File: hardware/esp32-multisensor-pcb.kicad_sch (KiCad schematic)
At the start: 19 parts, among them J1 SS-52400-002, J2 B2B-PH-SM4-TB, U2 MCP73871

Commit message: feat: add LDO voltage regulator and battery connector
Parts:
- added C3, C5: 0.1uF, symbol Device:C_Small
- added C4, C6: 10uF, symbol Device:C_Polarized_Small_US
- J2: value B2B-PH-SM4-TB -> LiPo
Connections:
- net +5V: now also VR1.3 (VIN), C3.1, C4.1
- net GND: now also J2.2, VR1.1 (GND), C3.2, C4.2, C5.2, C6.2
- net VBATT: now reaches U2.14 (V_{BAT}), U2.15 (V_{BAT}), U2.16 (V_{BAT_SENSE})
- net VBATT: now also J2.1
- net +3.3V: now reaches VR1.2 (VOUT_2)
- net +3.3V: now also VR1.4 (VOUT_4), C5.1, C6.1
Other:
- note added: "LiPo battery charger"
- note added: "Low Dropout(LDO)voltage regulator"
- note added: "USB connector"
- note removed: "LiPo Battery Charger"
- note removed: "USB Connector"
- moved on the sheet: D1, D2, D3, J2, R7, R8, R9

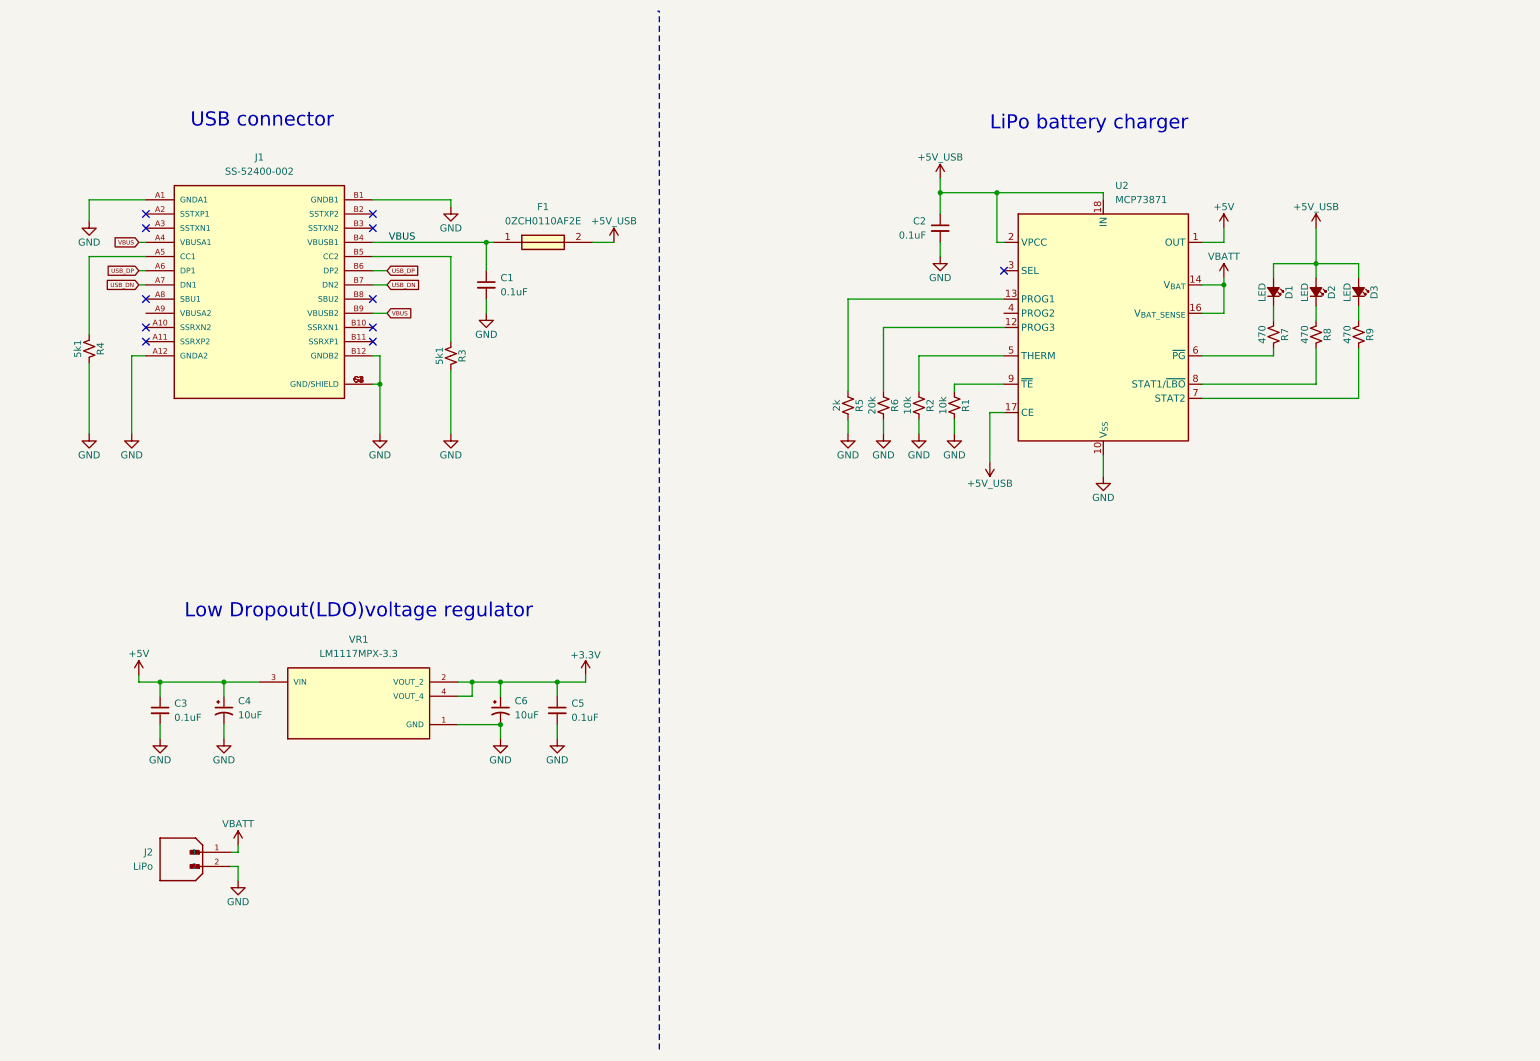
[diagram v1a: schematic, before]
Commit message: feat: add power LED indicator 3v3
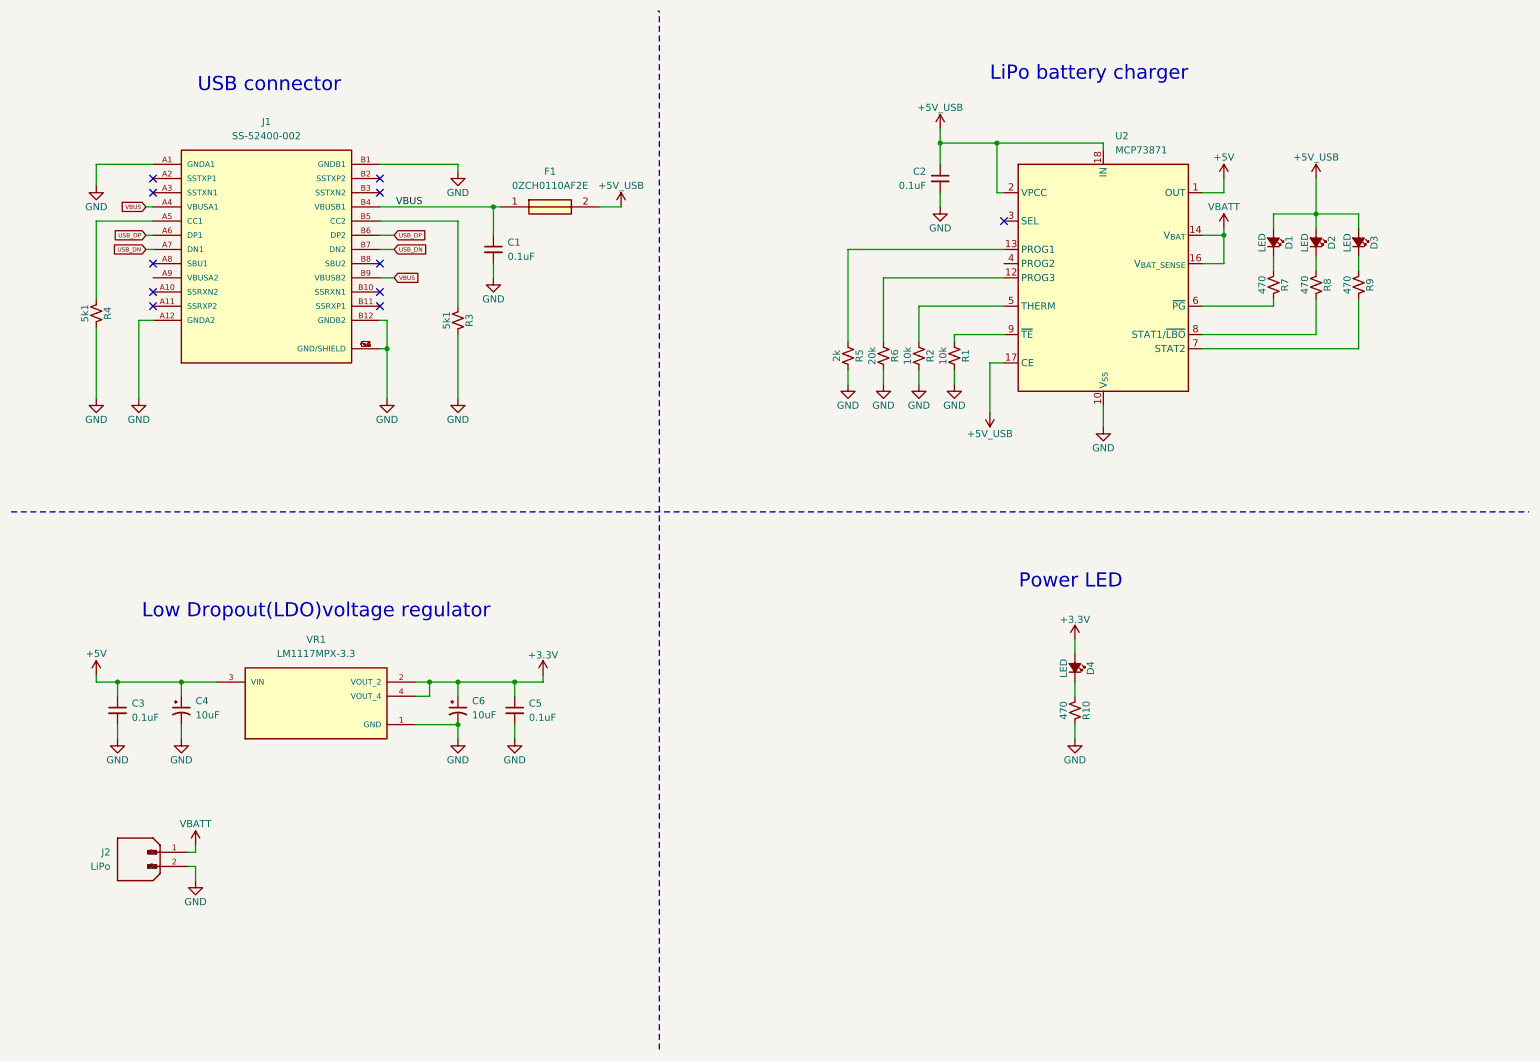
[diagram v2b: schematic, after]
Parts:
- added D4: LED, symbol Device:LED_Small_Filled
- added R10: 470, symbol Device:R_Small_US
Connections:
- net +3.3V: now also D4.2 (A)
- net GND: now also R10.2
- new net: D4.1 (K), R10.1
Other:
- note added: "Power LED"
- moved on the sheet: C1, C2, C3, C4, C5, C6, D1, D2, D3, F1, J1, J2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

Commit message: feat: add USB to serial connection
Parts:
- D1: value LED -> RED
- D2: value LED -> GREEN
- D3: value LED -> BLUE
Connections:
- net +5V_USB: now also U2.4 (PROG2)
- net CHARGED: now reaches R8.2, U2.8 (STAT1/~{LBO})
- net CHARGING: now reaches R7.2, U2.6 (~{PG})
- net CHARGING_POWER_GOOD: now reaches R9.2, U2.7 (STAT2)
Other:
- added sheet ESP32-C3-02 (esp32-c3-02.kicad_sch)
- moved on the sheet: D4, R10
